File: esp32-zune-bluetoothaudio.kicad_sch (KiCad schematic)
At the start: 12 parts

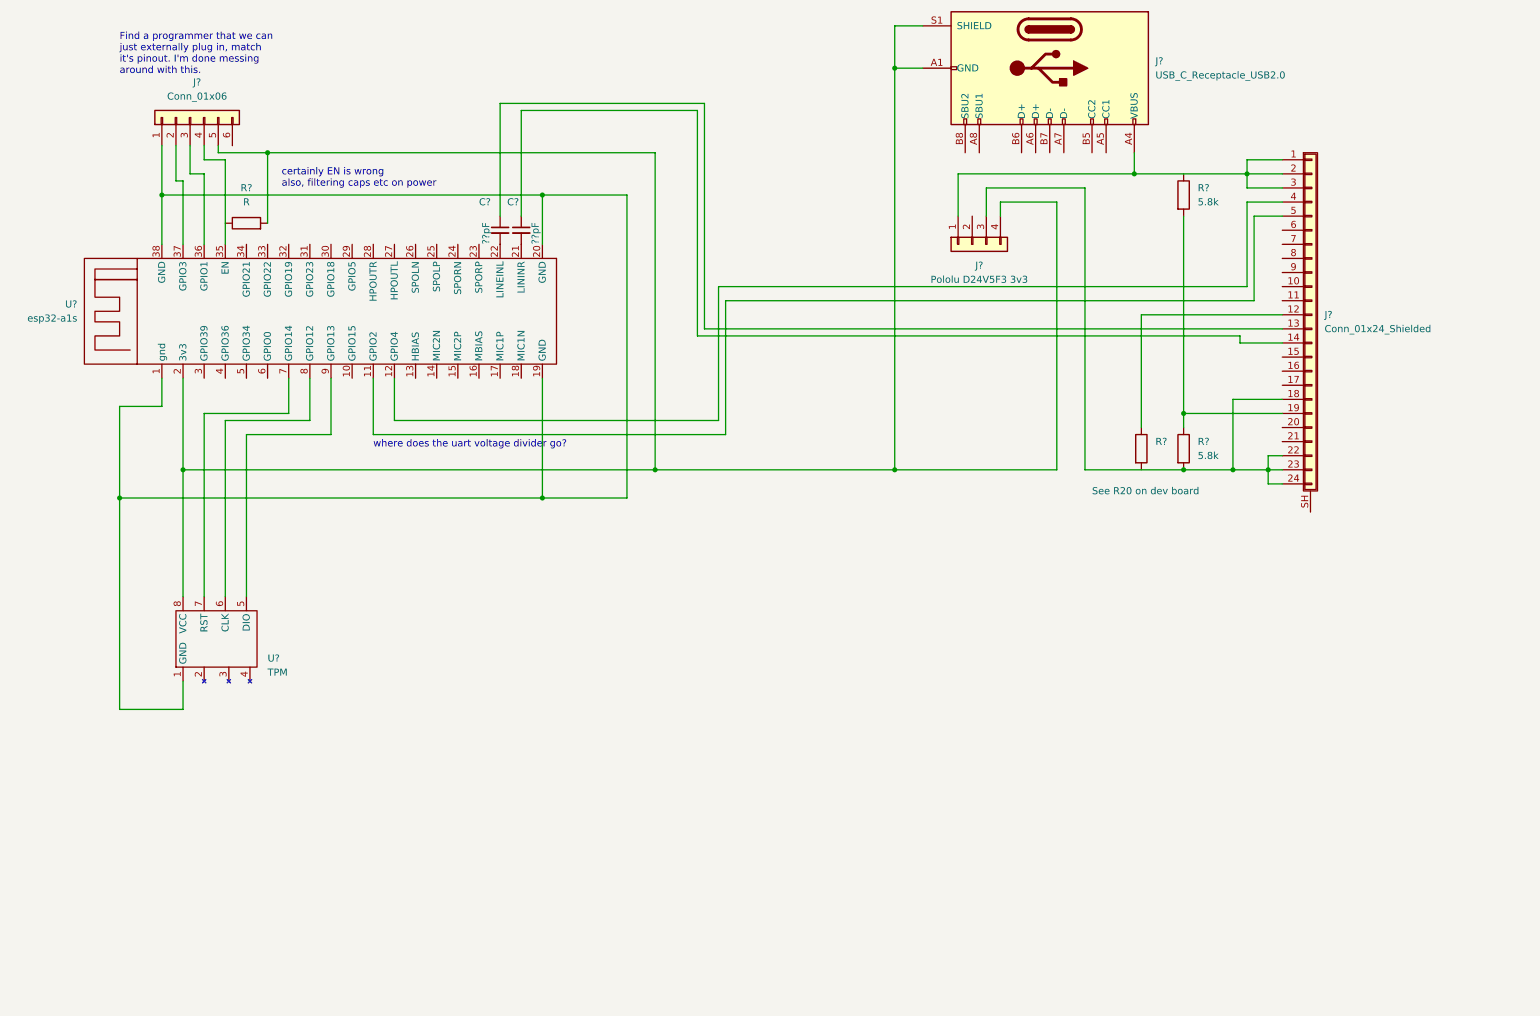
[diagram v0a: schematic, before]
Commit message: cleanup a bit, add level shifting
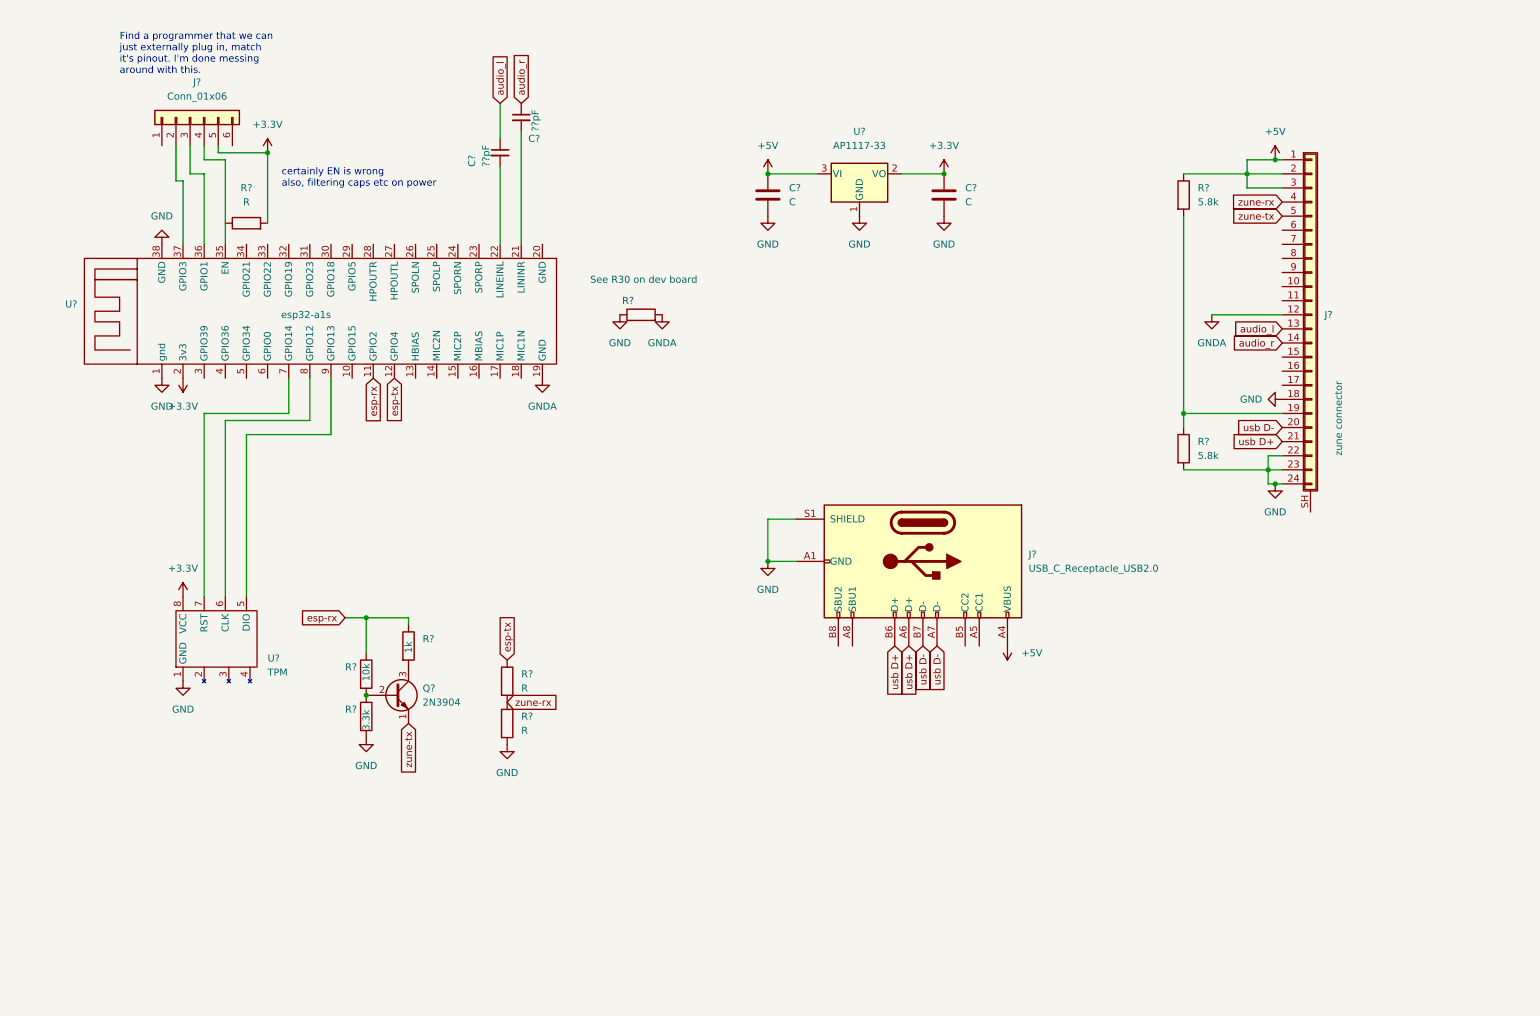
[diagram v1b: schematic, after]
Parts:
- removed J?: Pololu D24V5F3 3v3, symbol Connector_Generic:Conn_01x04
- added C? (x2): C, symbol Device:C
- added Q?: 2N3904, Package_TO_SOT_THT:TO-92_Inline, symbol Transistor_BJT:2N3904
- added R?: 3.3k, symbol Device:R
- added R?: 1k, symbol Device:R
- added R? (x2): R, symbol Device:R
- added R?: 10k, symbol Device:R
- added U?: AP1117-33, Package_TO_SOT_SMD:SOT-223-3_TabPin2, symbol Regulator_Linear:AP1117-33
- J?: value Conn_01x24_Shielded -> zune connector
- R?: value See R20 on dev board -> See R30 on dev board
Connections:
- net +5V: now reaches J?.1 (Pin_1), J?.2 (Pin_2), J?.3 (Pin_3), J?.A4 (VBUS), J?.A9 (VBUS), J?.B4 (VBUS), J?.B9 (VBUS)
- net +5V: now also R?.1, C?.1, U?.3 (VI)
- net GND: now reaches R?.1
- net GND: now also J?.18 (Pin_18), J?.22 (Pin_22), J?.23 (Pin_23), J?.24 (Pin_24), J?.A1 (GND), J?.A12 (GND), J?.B1 (GND), J?.B12 (GND), J?.S1 (SHIELD), R?.2, U?.1 (GND), U?.1 (gnd), U?.38 (GND), C?.2, C?.2, R?.2, R?.2, U?.1 (GND); no longer J?.12 (Pin_12)
- net audio_l: now reaches C?.1, J?.13 (Pin_13)
- net audio_r: now reaches C?.1, J?.14 (Pin_14)
- net usb D-: now reaches J?.20 (Pin_20)
- net usb D-: now also J?.A7 (D-), J?.B7 (D-)
- net usb D+: now reaches J?.21 (Pin_21)
- net usb D+: now also J?.A6 (D+), J?.B6 (D+)
- net esp-tx: now reaches U?.12 (GPIO4)
- net esp-tx: now also R?.1; no longer J?.4 (Pin_4)
- net esp-rx: now reaches U?.11 (GPIO2)
- net esp-rx: now also R?.1, R?.1; no longer J?.5 (Pin_5)
- net GNDA: now reaches R?.2
- net GNDA: now also J?.12 (Pin_12), U?.19 (GND)
- new net: Q?.2 (B), R?.1, R?.2
- new net: Q?.3 (C), R?.2
- new net +3.3V: C?.1, J?.5 (Pin_5), R?.2, U?.2 (3v3), U?.2 (VO), U?.8 (VCC)
- new net zune-rx: J?.4 (Pin_4), R?.1, R?.2
- new net zune-tx: J?.5 (Pin_5), Q?.1 (E)
- now unconnected: J?.1 (Pin_1), U?.20 (GND)
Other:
- note removed: "where does the uart voltage divider go?"
- moved on the sheet: C?, J?, R?

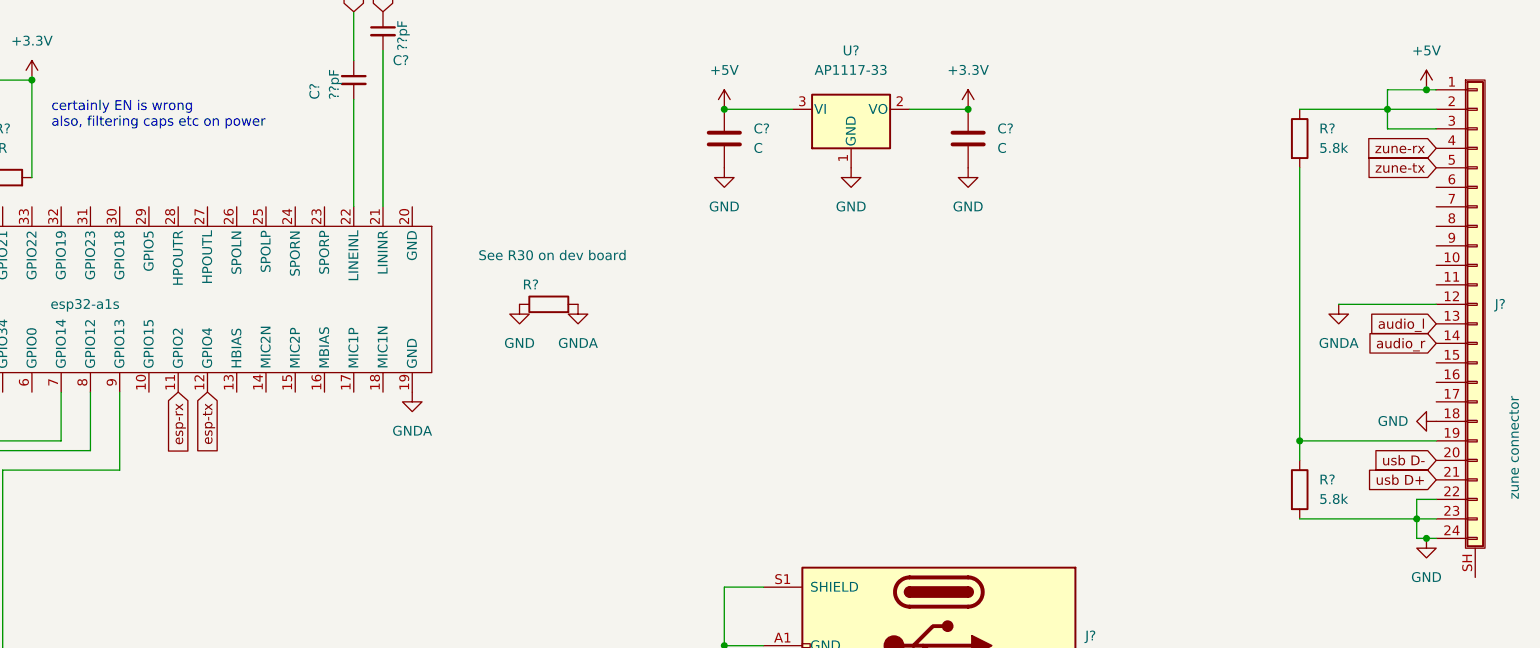
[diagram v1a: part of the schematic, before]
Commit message: update to represent the state of the breadboard
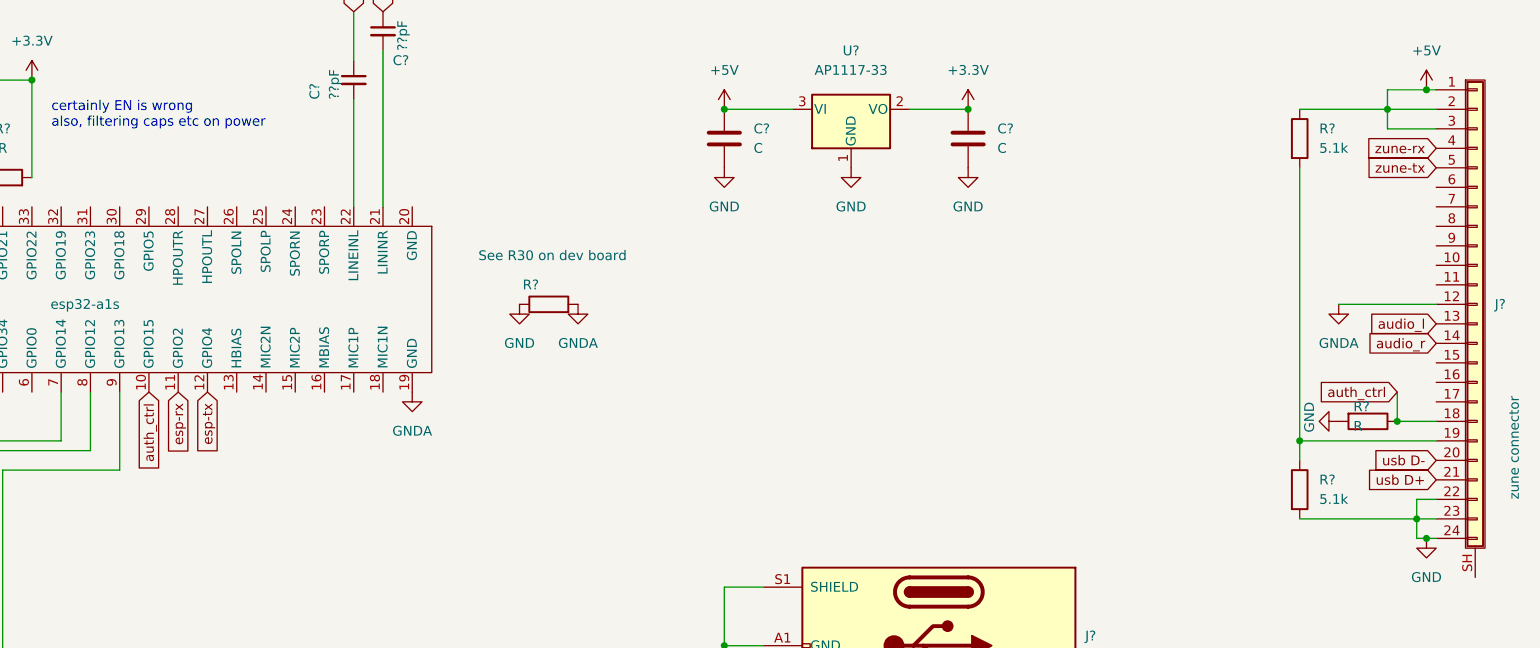
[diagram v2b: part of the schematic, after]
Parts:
- added R?: R, symbol Device:R
- R? (x2): value 5.8k -> 5.1k
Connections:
- net GND: now also R?.2; no longer J?.18 (Pin_18)
- net auth_ctrl: now reaches U?.10 (GPIO15)
- net auth_ctrl: now also J?.18 (Pin_18), R?.1
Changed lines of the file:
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@@
   (junction (at 69.85 125.73) (diameter 0) (color 0 0 0 0)
   )
+  (junction (at 229.87 86.36) (diameter 0) (color 0 0 0 0)
+  )
   (junction (at 217.17 88.9) (diameter 0) (color 0 0 0 0)
   )
@@
     (stroke (width 0) (type default) (color 0 0 0 0))
   )
+  (wire (pts (xy 229.87 86.36) (xy 234.95 86.36))
+    (stroke (width 0) (type default) (color 0 0 0 0))
+  )
   (wire (pts (xy 93.98 44.45) (xy 93.98 58.42))
+    (stroke (width 0) (type default) (color 0 0 0 0))
+  )
+  (wire (pts (xy 229.87 82.55) (xy 229.87 86.36))
     (stroke (width 0) (type default) (color 0 0 0 0))
   )
@@
     (effects (font (size 1.27 1.27)) (justify right))
     (property "Intersheet References" "${INTERSHEET_REFS}" (id 0) (at 224.7959 53.4194 0)
+      (effects (font (size 1.27 1.27)) (justify right) hide)
+    )
+  )
+  (global_label "auth_ctrl" (shape input) (at 229.87 82.55 180) (fields_autoplaced)
+    (effects (font (size 1.27 1.27)) (justify right))
+    (property "Intersheet References" "${INTERSHEET_REFS}" (id 0) (at 219.0507 82.4706 0)
       (effects (font (size 1.27 1.27)) (justify right) hide)
     )
@@
     (effects (font (size 1.27 1.27)) (justify right))
     (property "Intersheet References" "${INTERSHEET_REFS}" (id 0) (at 225.5821 76.2794 0)
+      (effects (font (size 1.27 1.27)) (justify right) hide)
+    )
+  )
+  (global_label "auth_ctrl" (shape input) (at 67.31 82.55 270) (fields_autoplaced)
+    (effects (font (size 1.27 1.27)) (justify right))
+    (property "Intersheet References" "${INTERSHEET_REFS}" (id 0) (at 67.2306 93.3693 90)
       (effects (font (size 1.27 1.27)) (justify right) hide)
     )
@@
     (pin "1")
   )
+  (symbol (lib_id "Device:R") (at 226.06 86.36 270) (unit 1)
+    (in_bom yes) (on_board yes)
+    (property "Reference" "R?" (id 0) (at 224.155 84.455 90)
+      (effects (font (size 1.27 1.27)) (justify left))
+    )
+    (property "Value" "R" (id 1) (at 224.155 86.995 90)
+      (effects (font (size 1.27 1.27)) (justify left))
+    )
+    (property "Footprint" "" (id 2) (at 226.06 84.582 90)
+      (effects (font (size 1.27 1.27)) hide)
+    )
+    (property "Datasheet" "~" (id 3) (at 226.06 86.36 0)
+      (effects (font (size 1.27 1.27)) hide)
+    )
+    (pin "1")
+    (pin "2")
+  )
   (symbol (lib_id "power:+3.3V") (at 36.83 82.55 180) (unit 1)
     (in_bom yes) (on_board yes) (fields_autoplaced)
@@
       (effects (font (size 1.27 1.27)) (justify left))
     )
-    (property "Value" "5.8k" (id 1) (at 219.71 50.7999 0)
+    (property "Value" "5.1k" (id 1) (at 219.71 50.7999 0)
       (effects (font (size 1.27 1.27)) (justify left))
     )
@@
       (effects (font (size 1.27 1.27)) (justify left))
     )
-    (property "Value" "5.8k" (id 1) (at 219.71 96.5199 0)
+    (property "Value" "5.1k" (id 1) (at 219.71 96.5199 0)
       (effects (font (size 1.27 1.27)) (justify left))
     )
@@
     (pin "3")
   )
+  (symbol (lib_id "power:GND") (at 222.25 86.36 270) (unit 1)
+    (in_bom yes) (on_board yes)
+    (property "Reference" "#PWR?" (id 0) (at 215.9 86.36 0)
+      (effects (font (size 1.27 1.27)) hide)
+    )
+    (property "Value" "GND" (id 1) (at 218.44 83.82 0)
+      (effects (font (size 1.27 1.27)) (justify left))
+    )
+    (property "Footprint" "" (id 2) (at 222.25 86.36 0)
+      (effects (font (size 1.27 1.27)) hide)
+    )
+    (property "Datasheet" "" (id 3) (at 222.25 86.36 0)
+      (effects (font (size 1.27 1.27)) hide)
+    )
+    (pin "1")
+  )
   (symbol (lib_id "power:GND") (at 33.02 82.55 0) (unit 1)
     (in_bom yes) (on_board yes) (fields_autoplaced)
@@
     )
     (property "Datasheet" "" (id 3) (at 33.02 82.55 0)
-      (effects (font (size 1.27 1.27)) hide)
-    )
-    (pin "1")
-  )
-  (symbol (lib_id "power:GND") (at 234.95 86.36 270) (unit 1)
-    (in_bom yes) (on_board yes)
-    (property "Reference" "#PWR?" (id 0) (at 228.6 86.36 0)
-      (effects (font (size 1.27 1.27)) hide)
-    )
-    (property "Value" "GND" (id 1) (at 227.33 86.36 90)
-      (effects (font (size 1.27 1.27)) (justify left))
-    )
-    (property "Footprint" "" (id 2) (at 234.95 86.36 0)
-      (effects (font (size 1.27 1.27)) hide)
-    )
-    (property "Datasheet" "" (id 3) (at 234.95 86.36 0)
       (effects (font (size 1.27 1.27)) hide)
     )
@@
       (reference "#PWR?") (unit 1) (value "GND") (footprint "")
     )
+    (path "/d045a9e6-a79e-4b81-b2be-58dfde1b4bc1"
+      (reference "#PWR?") (unit 1) (value "GND") (footprint "")
+    )
     (path "/d0a06d2e-d614-4690-8f1d-320e1032d7a6"
       (reference "#PWR?") (unit 1) (value "GND") (footprint "")
     )
-    (path "/d566c9e4-b485-4574-9a3b-3c67827742a0"
-      (reference "#PWR?") (unit 1) (value "GND") (footprint "")
-    )
     (path "/dccb2402-1b52-4f77-b465-d5e62830b796"
       (reference "#PWR?") (unit 1) (value "GND") (footprint "")
@@
       (reference "Q?") (unit 1) (value "2N3904") (footprint "Package_TO_SOT_THT:TO-92_Inline")
     )
+    (path "/1a826a63-920f-4965-b510-4173b803ad4f"
+      (reference "R?") (unit 1) (value "R") (footprint "")
+    )
     (path "/380f30bf-1ec9-4a0c-9c5b-60a9b93eb00b"
       (reference "R?") (unit 1) (value "3.3k") (footprint "")
     )
     (path "/40e096ce-9d6e-482d-b8c4-3ca126a99030"
-      (reference "R?") (unit 1) (value "5.8k") (footprint "")
+      (reference "R?") (unit 1) (value "5.1k") (footprint "")
     )
     (path "/6e0a5e0c-fe95-4f96-a7d3-ae4f8b21eb7d"
@@
     )
     (path "/c0dd6ac2-9de8-4163-a07c-d1d90bc3cd51"
-      (reference "R?") (unit 1) (value "5.8k") (footprint "")
+      (reference "R?") (unit 1) (value "5.1k") (footprint "")
     )
     (path "/d837d52a-3316-4f22-8429-329ad0002bff"
